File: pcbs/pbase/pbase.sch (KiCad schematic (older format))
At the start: 0 parts

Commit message: cambios a sch
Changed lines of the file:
@@
 F0 "Zigbee" 60
 F1 "Zigbee.sch" 60
-F2 "RXD2" O L 7250 2450 60
-F3 "TXD2" I L 7250 2550 60
-F4 "SLRQ" I L 7250 2950 60
-F5 "SLEEP" O L 7250 2850 60
-F6 "CTS" O L 7250 2650 60
-F7 "RSSI" O L 7250 3050 60
-F8 "RTS" I L 7250 2750 60
+F2 "SLRQ" I L 7250 2950 60
+F3 "SLEEP" O L 7250 2850 60
+F4 "CTS" O L 7250 2650 60
+F5 "RSSI" O L 7250 3050 60
+F6 "RTS" I L 7250 2750 60
+F7 "RXD1" O L 7250 2450 60
+F8 "TXD1" I L 7250 2550 60
 $EndSheet
 $Sheet

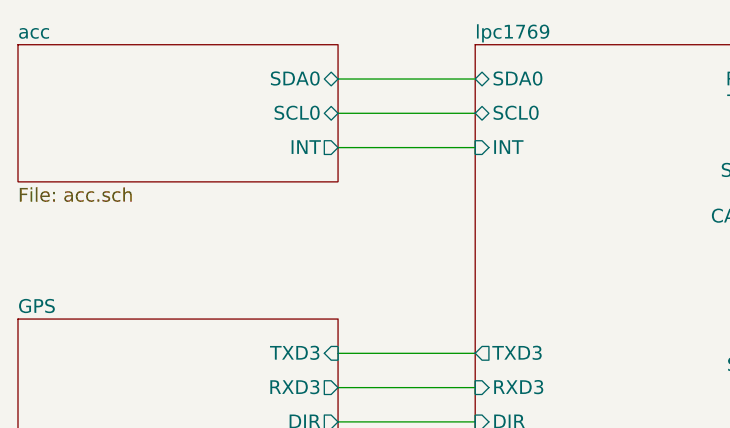
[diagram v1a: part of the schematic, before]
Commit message: reemplazado acc por mpu9250
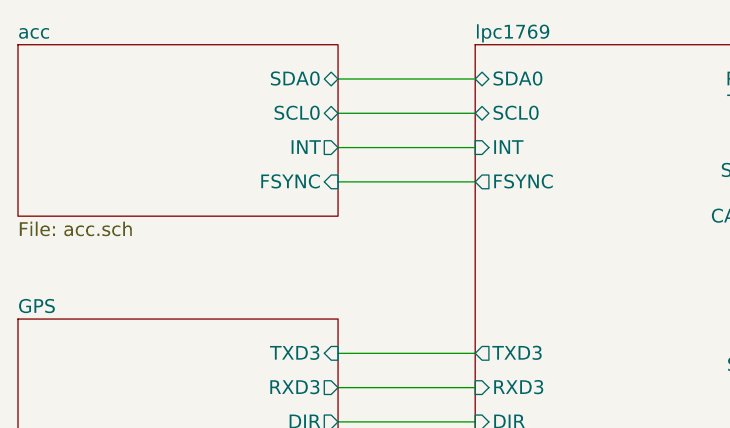
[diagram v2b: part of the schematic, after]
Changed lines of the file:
@@
 LIBS:lpcxpresso_lpc1769_revb
 LIBS:gps_em506
+LIBS:acc_mpu9250_board
 LIBS:pbase-cache
 EELAYER 25 0
@@
 F19 "SRQ" O R 6650 2950 60
 F20 "RTS1" O R 6650 2750 60
+F21 "FSYNC" O L 5250 2900 60
 $EndSheet
 $Sheet
@@
 $EndSheet
 $Sheet
-S 3250 2300 1400 600
+S 3250 2300 1400 750
 U 5B95B001
 F0 "acc" 60
@@
 F3 "SDA0" B R 4650 2450 60
 F4 "SCL0" B R 4650 2600 60
+F5 "FSYNC" I R 4650 2900 60
 $EndSheet
 $Sheet
@@
 Wire Wire Line
 	5250 3950 4650 3950
+Wire Wire Line
+	5250 2900 4650 2900
 $EndSCHEMATC

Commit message: pdfs realizados
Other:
- note added: "PER4MANCE"
- note added: "Placa base - lpc1769"
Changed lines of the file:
@@
 Sheet 1 8
 Title "Diagrama de bloques "
-Date "2018-09-17"
+Date "2018-10-30"
 Rev "A"
 Comp "UTN - FRBA"
-Comment1 ""
-Comment2 ""
-Comment3 "Utiliza acelerómetro MPU-9250"
-Comment4 "PLACA BASE"
+Comment1 "https://github.com/ealegremendoza/proyecto_4to"
+Comment2 "Autores: Alegre M. E., Bautista L., Tarazona L."
+Comment3 "Medidor de posición y velocidad de sujetos en movimiento."
+Comment4 "Sport Tracker"
 $EndDescr
 $Sheet
-S 5250 2300 1400 3150
+S 5050 2400 1400 3150
 U 5B95AFB2
 F0 "lpc1769" 60
 F1 "lpc1769.sch" 60
-F2 "MOSI1" B R 6650 5000 60
-F3 "MISO1" B R 6650 5100 60
-F4 "SCK1" B R 6650 5200 60
-F5 "SSEL1" B R 6650 5300 60
-F6 "TXD3" O L 5250 3650 60
-F7 "RXD3" I L 5250 3800 60
-F8 "DIR" I L 5250 3950 60
-F9 "SDA0" B L 5250 2450 60
-F10 "SCL0" B L 5250 2600 60
-F11 "INT" I L 5250 2750 60
-F12 "CAP2.1" I R 6650 3050 60
-F13 "SDA2" B R 6650 3700 60
-F14 "SCL2" B R 6650 3900 60
-F15 "TXD1" O R 6650 2550 60
-F16 "RXD1" I R 6650 2450 60
-F17 "CTS1" I R 6650 2650 60
-F18 "SLEEP" I R 6650 2850 60
-F19 "SRQ" O R 6650 2950 60
-F20 "RTS1" O R 6650 2750 60
-F21 "FSYNC" O L 5250 2900 60
+F2 "MOSI1" B R 6450 5100 60
+F3 "MISO1" B R 6450 5200 60
+F4 "SCK1" B R 6450 5300 60
+F5 "SSEL1" B R 6450 5400 60
+F6 "TXD3" O L 5050 3750 60
+F7 "RXD3" I L 5050 3900 60
+F8 "DIR" I L 5050 4050 60
+F9 "SDA0" B L 5050 2550 60
+F10 "SCL0" B L 5050 2700 60
+F11 "INT" I L 5050 2850 60
+F12 "CAP2.1" I R 6450 3150 60
+F13 "SDA2" B R 6450 3800 60
+F14 "SCL2" B R 6450 4000 60
+F15 "TXD1" O R 6450 2650 60
+F16 "RXD1" I R 6450 2550 60
+F17 "CTS1" I R 6450 2750 60
+F18 "SLEEP" I R 6450 2950 60
+F19 "SRQ" O R 6450 3050 60
+F20 "RTS1" O R 6450 2850 60
+F21 "FSYNC" O L 5050 3000 60
 $EndSheet
 $Sheet
-S 7250 2300 1400 850
+S 7050 2400 1400 850
 U 5B95AFE6
 F0 "Zigbee" 60
 F1 "Zigbee.sch" 60
-F2 "SLRQ" I L 7250 2950 60
-F3 "SLEEP" O L 7250 2850 60
-F4 "CTS" O L 7250 2650 60
-F5 "RSSI" O L 7250 3050 60
-F6 "RTS" I L 7250 2750 60
-F7 "RXD1" O L 7250 2450 60
-F8 "TXD1" I L 7250 2550 60
+F2 "SLRQ" I L 7050 3050 60
+F3 "SLEEP" O L 7050 2950 60
+F4 "CTS" O L 7050 2750 60
+F5 "RSSI" O L 7050 3150 60
+F6 "RTS" I L 7050 2850 60
+F7 "RXD1" O L 7050 2550 60
+F8 "TXD1" I L 7050 2650 60
 $EndSheet
 $Sheet
-S 3250 2300 1400 750
+S 3050 2400 1400 750
 U 5B95B001
 F0 "acc" 60
 F1 "acc.sch" 60
-F2 "INT" O R 4650 2750 60
-F3 "SDA0" B R 4650 2450 60
-F4 "SCL0" B R 4650 2600 60
-F5 "FSYNC" I R 4650 2900 60
+F2 "INT" O R 4450 2850 60
+F3 "SDA0" B R 4450 2550 60
+F4 "SCL0" B R 4450 2700 60
+F5 "FSYNC" I R 4450 3000 60
 $EndSheet
 $Sheet
-S 3250 3500 1400 600
+S 3050 3600 1400 600
 U 5B95B01D
 F0 "GPS" 60
 F1 "GPS.sch" 60
-F2 "DIR" O R 4650 3950 60
-F3 "RXD3" O R 4650 3800 60
-F4 "TXD3" I R 4650 3650 60
+F2 "DIR" O R 4450 4050 60
+F3 "RXD3" O R 4450 3900 60
+F4 "TXD3" I R 4450 3750 60
 $EndSheet
 $Sheet
-S 7250 4850 1400 600
+S 7050 4950 1400 600
 U 5B95B035
 F0 "TarjetaSD" 60
 F1 "TarjetaSD.sch" 60
-F2 "SSEL1" I L 7250 5300 60
-F3 "MOSI1" I L 7250 5000 60
-F4 "MISO1" O L 7250 5100 60
-F5 "SCK1" I L 7250 5200 60
+F2 "SSEL1" I L 7050 5400 60
+F3 "MOSI1" I L 7050 5100 60
+F4 "MISO1" O L 7050 5200 60
+F5 "SCK1" I L 7050 5300 60
 $EndSheet
 $Sheet
-S 7250 3500 1400 600
+S 7050 3600 1400 600
 U 5B95B180
 F0 "Display" 60
 F1 "Display.sch" 60
-F2 "SDA2" B L 7250 3700 60
-F3 "SCL2" B L 7250 3900 60
+F2 "SDA2" B L 7050 3800 60
+F3 "SCL2" B L 7050 4000 60
 $EndSheet
 $Sheet
-S 3250 4850 1400 600
+S 3050 4950 1400 600
 U 5B95B241
 F0 "Alimentación" 60
@@
 $EndSheet
 Wire Wire Line
-	7250 2450 6650 2450
+	7050 2550 6450 2550
 Wire Wire Line
-	6650 2550 7250 2550
+	6450 2650 7050 2650
 Wire Wire Line
-	7250 2650 6650 2650
+	7050 2750 6450 2750
 Wire Wire Line
-	6650 2750 7250 2750
+	6450 2850 7050 2850
 Wire Wire Line
-	7250 2850 6650 2850
+	7050 2950 6450 2950
 Wire Wire Line
-	6650 2950 7250 2950
+	6450 3050 7050 3050
 Wire Wire Line
-	7250 3050 6650 3050
+	7050 3150 6450 3150
 Wire Wire Line
-	7250 5000 6650 5000
+	7050 5100 6450 5100
 Wire Wire Line
-	7250 5100 6650 5100
+	7050 5200 6450 5200
 Wire Wire Line
-	7250 5200 6650 5200
+	7050 5300 6450 5300
 Wire Wire Line
-	7250 5300 6650 5300
+	7050 5400 6450 5400
 Wire Wire Line
-	7250 3700 6650 3700
+	7050 3800 6450 3800
 Wire Wire Line
-	6650 3900 7250 3900
+	6450 4000 7050 4000
 Wire Wire Line
-	4650 2450 5250 2450
+	4450 2550 5050 2550
 Wire Wire Line
-	5250 2600 4650 2600
+	5050 2700 4450 2700
 Wire Wire Line
-	4650 2750 5250 2750
+	4450 2850 5050 2850
 Wire Wire Line
-	5250 3650 4650 3650
+	5050 3750 4450 3750
 Wire Wire Line
-	4650 3800 5250 3800
+	4450 3900 5050 3900
 Wire Wire Line
-	5250 3950 4650 3950
+	5050 4050 4450 4050
 Wire Wire Line
-	5250 2900 4650 2900
+	5050 3000 4450 3000
+Text Notes 5050 1450 0    157  ~ 31
+PER4MANCE
+Text Notes 5050 1750 0    79   ~ 0
+Placa base - lpc1769
 $EndSCHEMATC
